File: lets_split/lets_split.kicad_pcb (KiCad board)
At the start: 2 copper layers, 112 x 79 mm, 64 parts, among them J1 3PIN, J2 6PIN, J3 3PIN, J4 CON1, SW1 SW_PUSH, SW10 SW_PUSH, SW11 SW_PUSH, SW12 SW_PUSH, SW13 SW_PUSH, SW14 SW_PUSH, SW15 SW_PUSH, SW16 SW_PUSH, SW17 SW_PUSH, SW18 SW_PUSH, SW19 SW_PUSH, SW2 SW_PUSH, SW20 SW_PUSH, SW21 SW_PUSH, SW22 SW_PUSH, SW23 SW_PUSH, SW24 SW_PUSH, SW3 SW_PUSH, SW4 SW_PUSH, SW5 SW_PUSH, SW6 SW_PUSH, SW7 SW_PUSH, SW8 SW_PUSH, SW9 SW_PUSH, U1 ProMicro, U2 HOLE, U3 HOLE, U4 HOLE, U5 HOLE

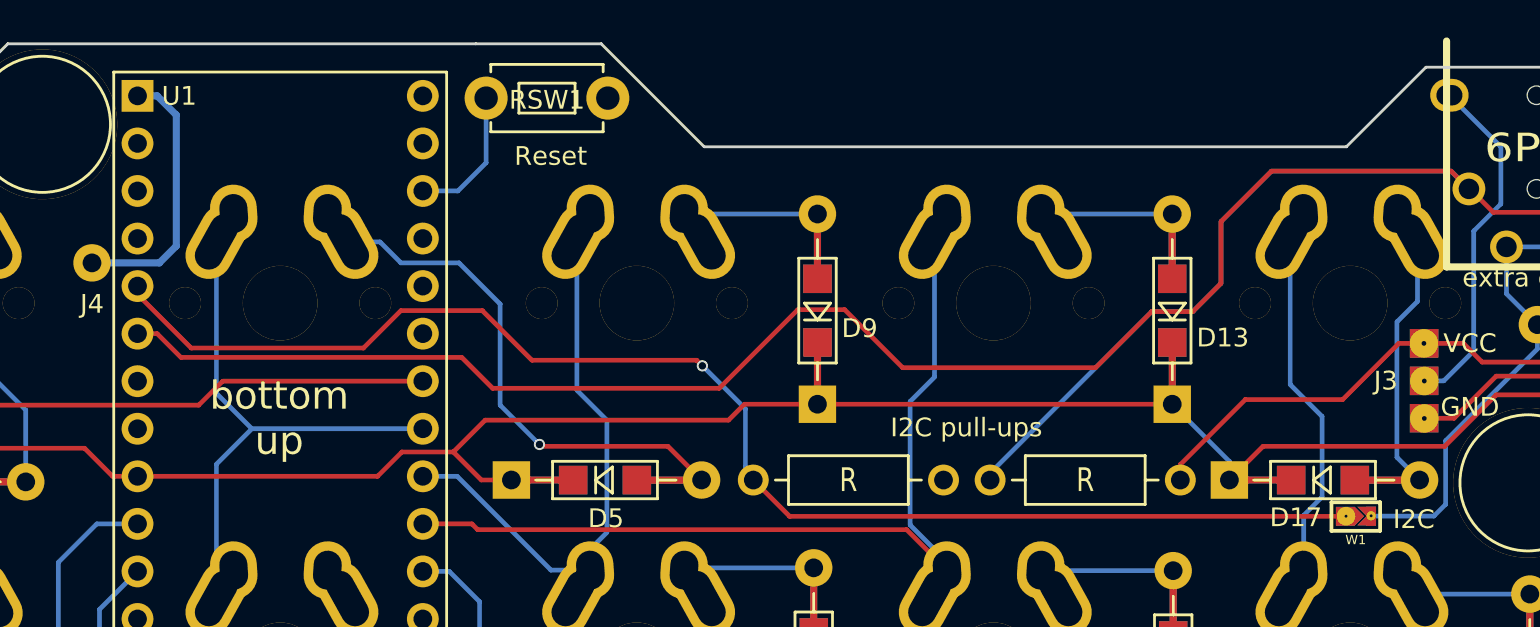
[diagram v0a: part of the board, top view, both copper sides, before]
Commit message: Change bottom fill from VCC to GND
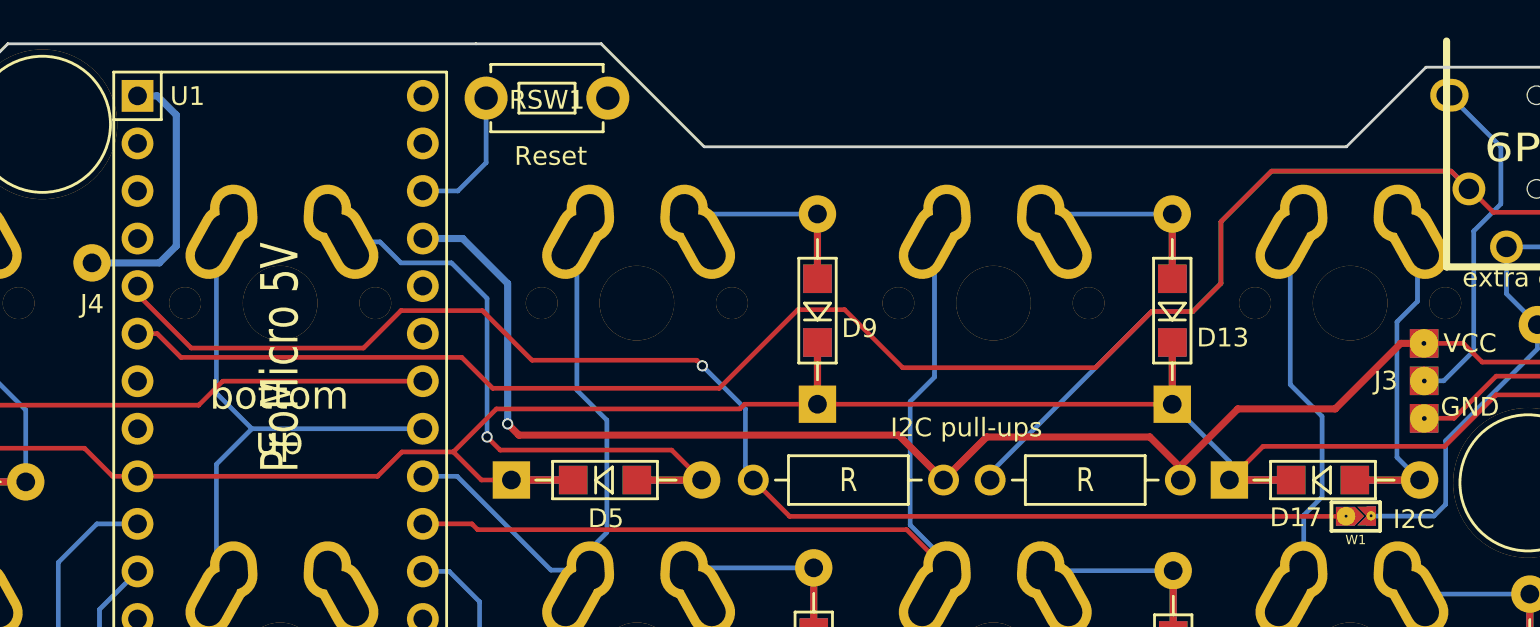
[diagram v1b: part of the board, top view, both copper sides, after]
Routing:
- net VCC: track 29.1 -> 81.5 mm, vias 0 -> 1
- net Net-(D5-Pad2): track 34.3 -> 35.4 mm
- added copper zone on B.Cu, net GND
- removed copper zone on B.Cu, net VCC

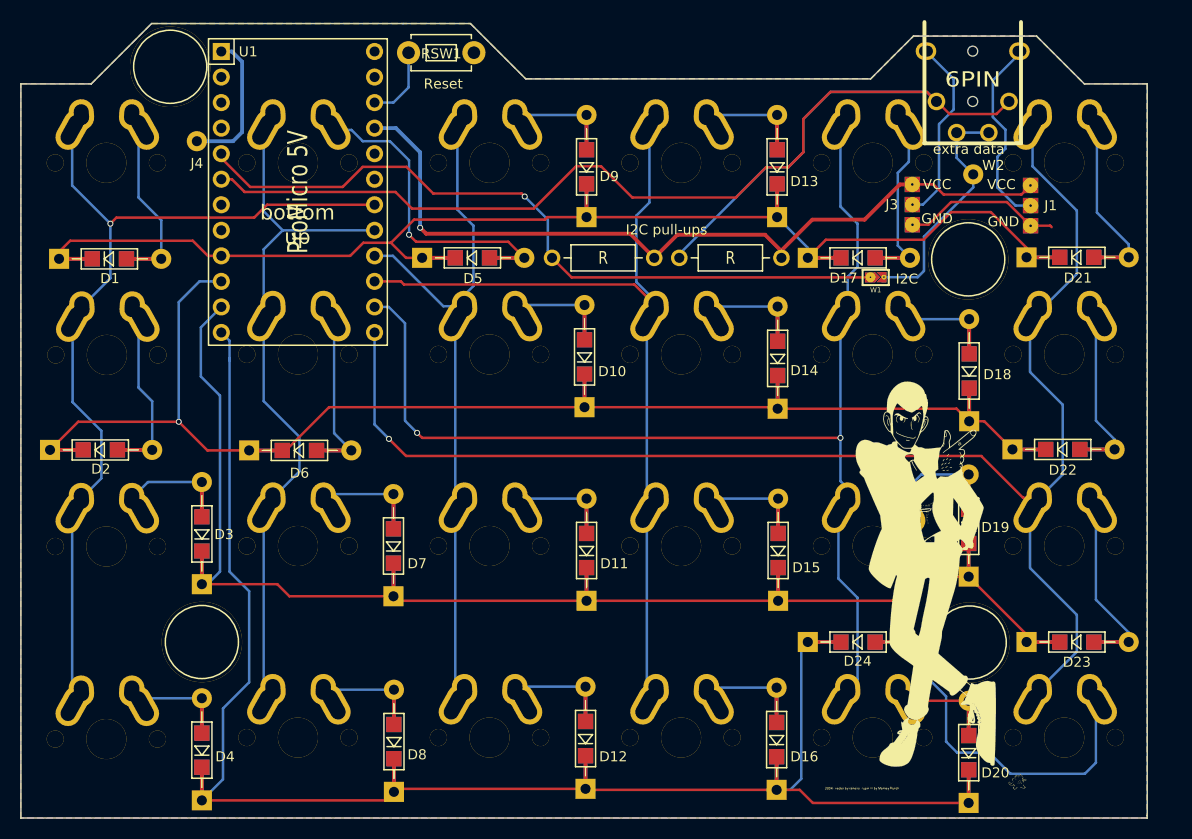
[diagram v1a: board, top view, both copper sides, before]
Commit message: Add pads for RGB LED strip which uses WS2812B for underglow
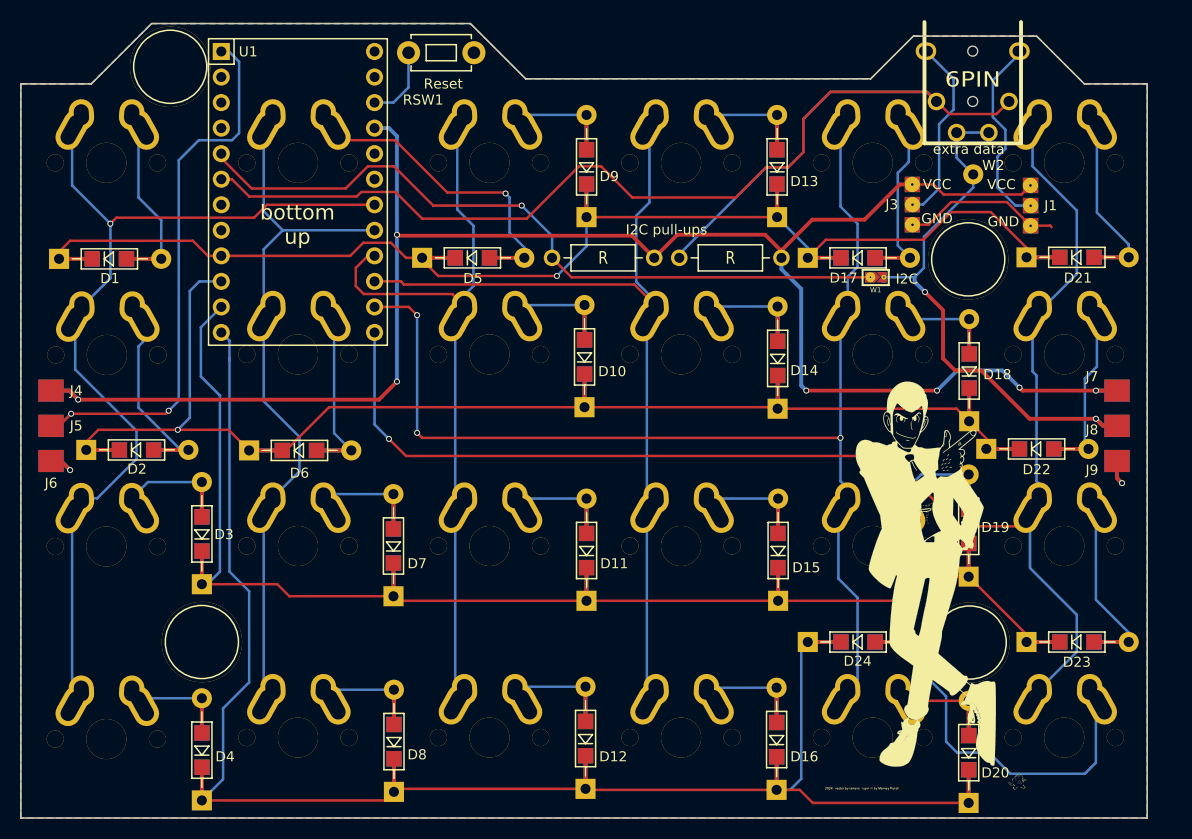
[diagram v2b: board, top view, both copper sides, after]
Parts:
- added J5: CON1, local:CON1_SMD_BOTH, F.Cu at (40.0, 73.0)
- added J6: CON1, local:CON1_SMD_BOTH, F.Cu at (40.0, 76.5)
- added J7: CON1, local:CON1_SMD_BOTH, F.Cu at (146.0, 69.5)
- added J8: CON1, local:CON1_SMD_BOTH, F.Cu at (146.0, 73.0)
- added J9: CON1, local:CON1_SMD_BOTH, F.Cu at (146.0, 76.5)
- J4: footprint local:CON1 -> local:CON1_SMD_BOTH
- moved J4 28.7 mm to (40.0, 69.5)
- moved D2 3.60 mm to (43.5, 75.4)
- moved D22 2.60 mm to (133.0, 75.3)
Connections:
- J4 pad 1: Net-(J4-Pad1) -> VCC
- U1 pad 1: Net-(J4-Pad1) -> Net-(J5-Pad1)
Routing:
- net VCC: track 81.5 -> 184.9 mm, vias 1 -> 7
- net Net-(J5-Pad1): track 0.00 -> 56.5 mm, vias 0 -> 2
- net xtradata: track 23.9 -> 55.4 mm, vias 0 -> 2
- net Net-(J4-Pad1): track 14.4 -> 0.00 mm
- net GND: track 15.8 -> 25.2 mm, vias 0 -> 2
- net row1: track 158.0 -> 153.0 mm
- net col2: track 65.5 -> 70.3 mm
- net col0: track 84.9 -> 88.7 mm
- net Net-(D2-Pad2): track 20.4 -> 22.3 mm
- net Net-(D5-Pad2): track 35.4 -> 33.8 mm
- net data: track 125.2 -> 126.4 mm
- net col4: track 112.8 -> 113.9 mm, vias 2 -> 3
- net col5: track 140.4 -> 139.3 mm
- net row0: track 149.5 -> 150.3 mm, vias 0 -> 1
- net I2C_SDA: track 73.5 -> 73.0 mm
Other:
- board text added: "J5"
- board text added: "J6"
- board text added: "J7"
- board text added: "J8"
- board text added: "J9"

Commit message: Simplify jumper for pin selection of TSSR jack
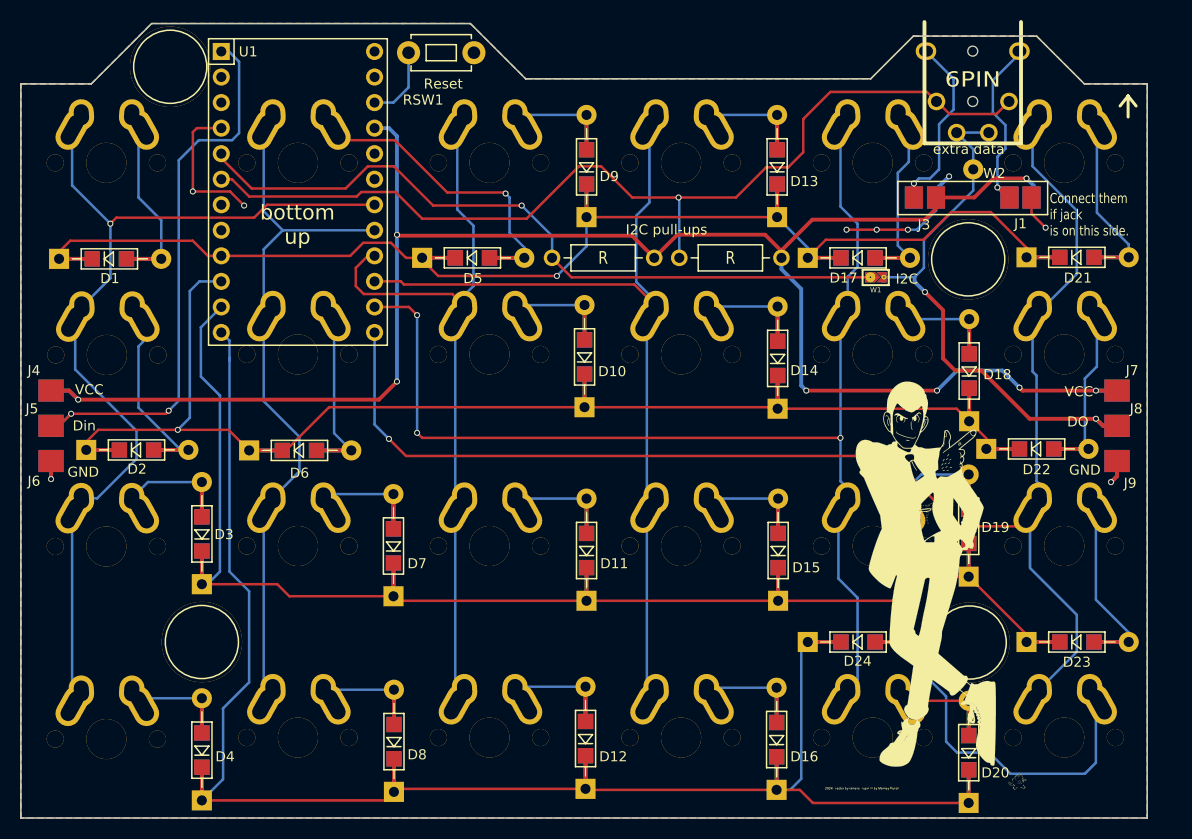
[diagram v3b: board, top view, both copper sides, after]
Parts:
- J1: footprint prettylib:jumper -> local:SMD_JUMPER_2
- J3: footprint prettylib:jumper -> local:SMD_JUMPER_2; moved to B.Cu
- moved J1 3.10 mm to (136.4, 50.3), turned to 0 degrees
- moved J3 1.03 mm to (126.9, 50.3), turned to 0 degrees
- moved W2 0.50 mm to (131.7, 47.5)
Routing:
- net data: track 126.4 -> 97.5 mm, vias 0 -> 1
- net GND: track 25.2 -> 40.0 mm, vias 2 -> 9
- net VCC: track 184.9 -> 187.1 mm, vias 7 -> 8
- net Net-(J1-Pad2): track 19.5 -> 18.7 mm, vias 0 -> 1
- net Net-(J2-Pad4): track 18.7 -> 19.4 mm, vias 0 -> 1
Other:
- board text added: "Connect them if jack is on this side."
- board text added: "DO"
- board text added: "Designed by Wootpatoot"
- board text added: "Din"
- board text added: "J1"
- board text added: "J3"
- board text removed: "By Wootpatoot"

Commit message: Add some GND fill
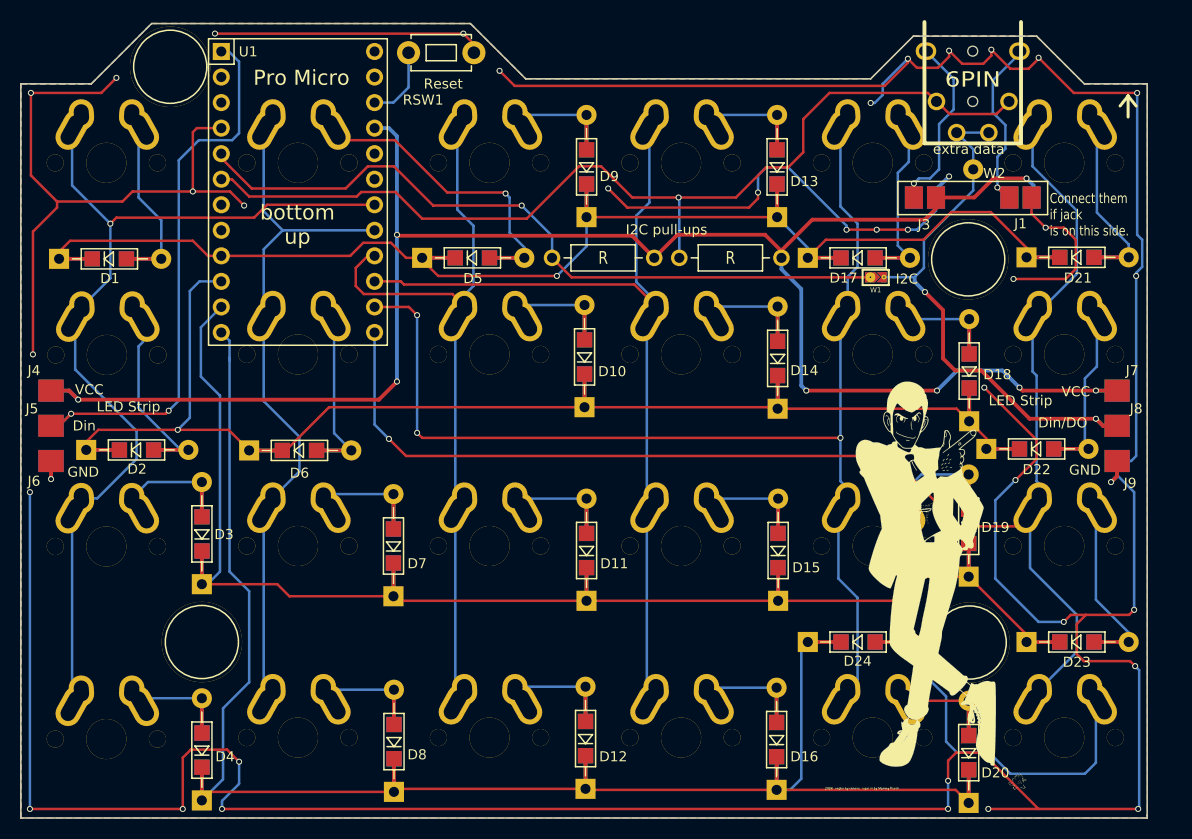
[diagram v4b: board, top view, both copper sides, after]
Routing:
- net GND: track 40.0 -> 523.9 mm, vias 9 -> 39
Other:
- board text added: "DO/Din"
- board text added: "Din/DO"
- board text added: "LED Strip"
- board text added: "Pro Micro"
- board text added: "U1"
- board text removed: "DO"

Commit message: Replace switch module without oval holes
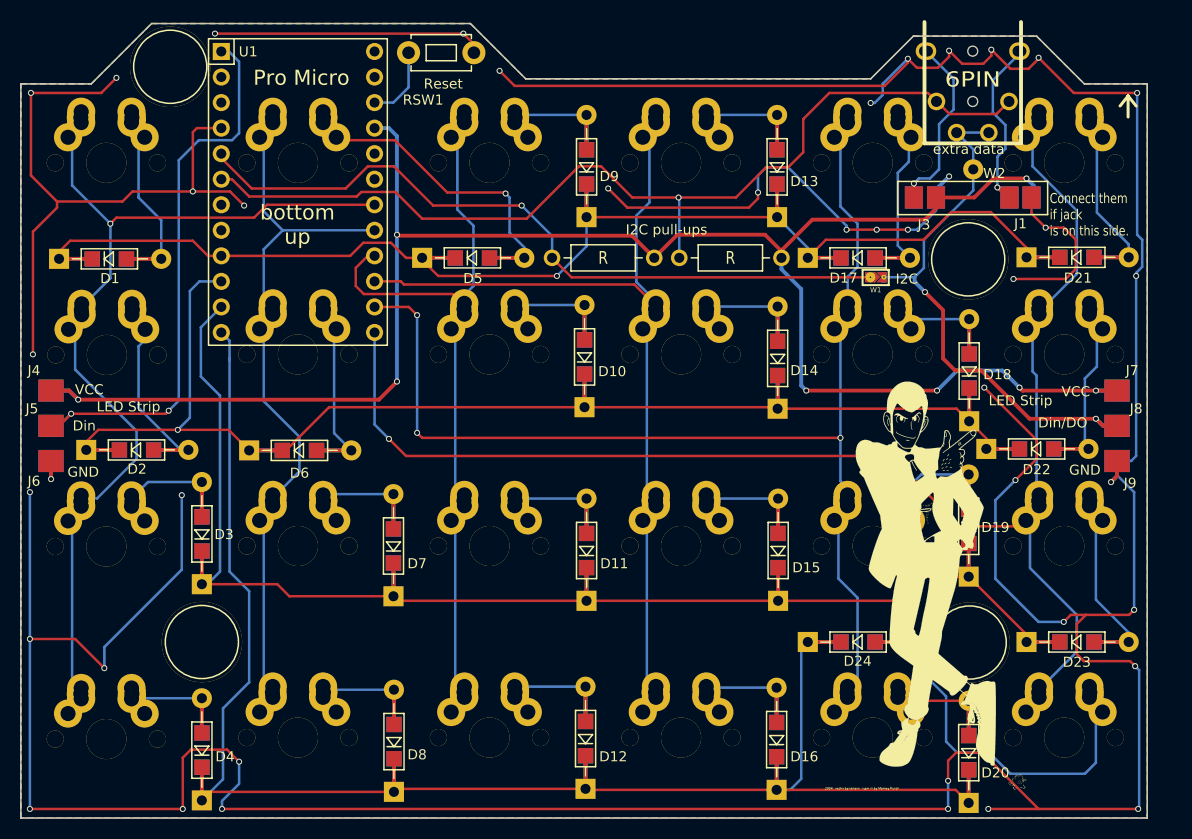
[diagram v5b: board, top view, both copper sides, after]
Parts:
- SW1, SW10, SW11, SW12, SW13, SW14, SW15, SW16, SW17, SW18, SW19, SW2, SW20, SW21, SW22, SW23, SW24, SW3, SW4, SW5, SW6, SW7, SW8, SW9: footprint flipalps:MXALPS_FLIP -> local:MXALPS_FLIP_HOLES
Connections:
- U1 pad 19: (no net) -> Net-(U1-Pad19)
- U1 pad 2: (no net) -> Net-(U1-Pad2)
- U1 pad 20: (no net) -> Net-(U1-Pad20)
- U1 pad 24: (no net) -> Net-(U1-Pad24)
- U1 pad 7: (no net) -> Net-(U1-Pad7)
- U1 pad 8: (no net) -> Net-(U1-Pad8)
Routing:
- net GND: track 523.9 -> 552.9 mm, vias 39 -> 42
- net col5: track 139.3 -> 141.8 mm
- net col2: track 70.3 -> 72.8 mm
- net col1: track 66.6 -> 69.1 mm
- net col0: track 88.7 -> 91.2 mm
- net col3: track 83.8 -> 86.3 mm
- net col4: track 113.9 -> 116.4 mm

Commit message: Add fiducial marks
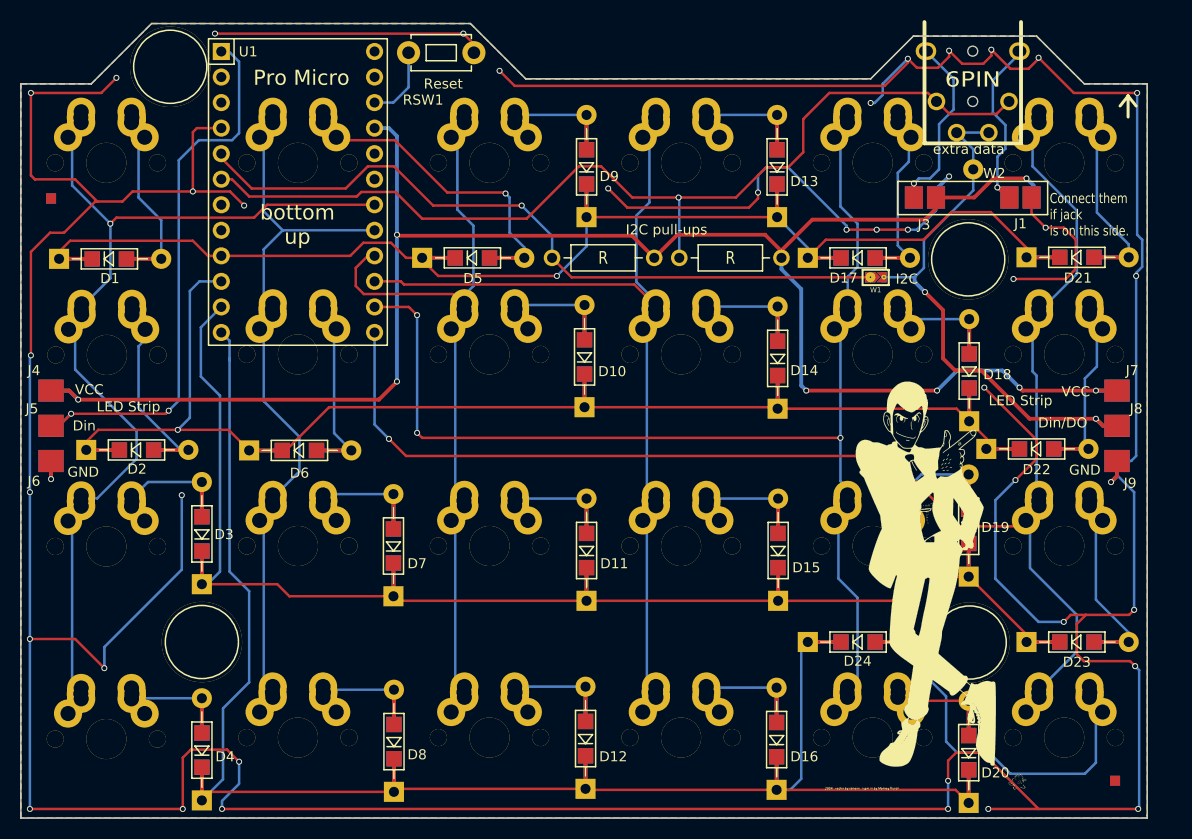
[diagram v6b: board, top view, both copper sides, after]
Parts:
- added M1: FIDUCIAL, local:Fiducial_Mark, F.Cu at (40.0, 50.4)
- added M2: FIDUCIAL, local:Fiducial_Mark, F.Cu at (145.8, 108.3)
- added M3: FIDUCIAL, local:Fiducial_Mark, B.Cu at (145.8, 108.3)
- added M4: FIDUCIAL, local:Fiducial_Mark, B.Cu at (40.0, 50.4)
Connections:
- U1 pad 19: Net-(U1-Pad19) -> (no net)
- U1 pad 2: Net-(U1-Pad2) -> (no net)
- U1 pad 20: Net-(U1-Pad20) -> (no net)
- U1 pad 24: Net-(U1-Pad24) -> (no net)
- U1 pad 7: Net-(U1-Pad7) -> (no net)
- U1 pad 8: Net-(U1-Pad8) -> (no net)
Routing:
- net GND: track 552.9 -> 569.3 mm

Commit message: Fix to match the distance between switch and side edge on both sides
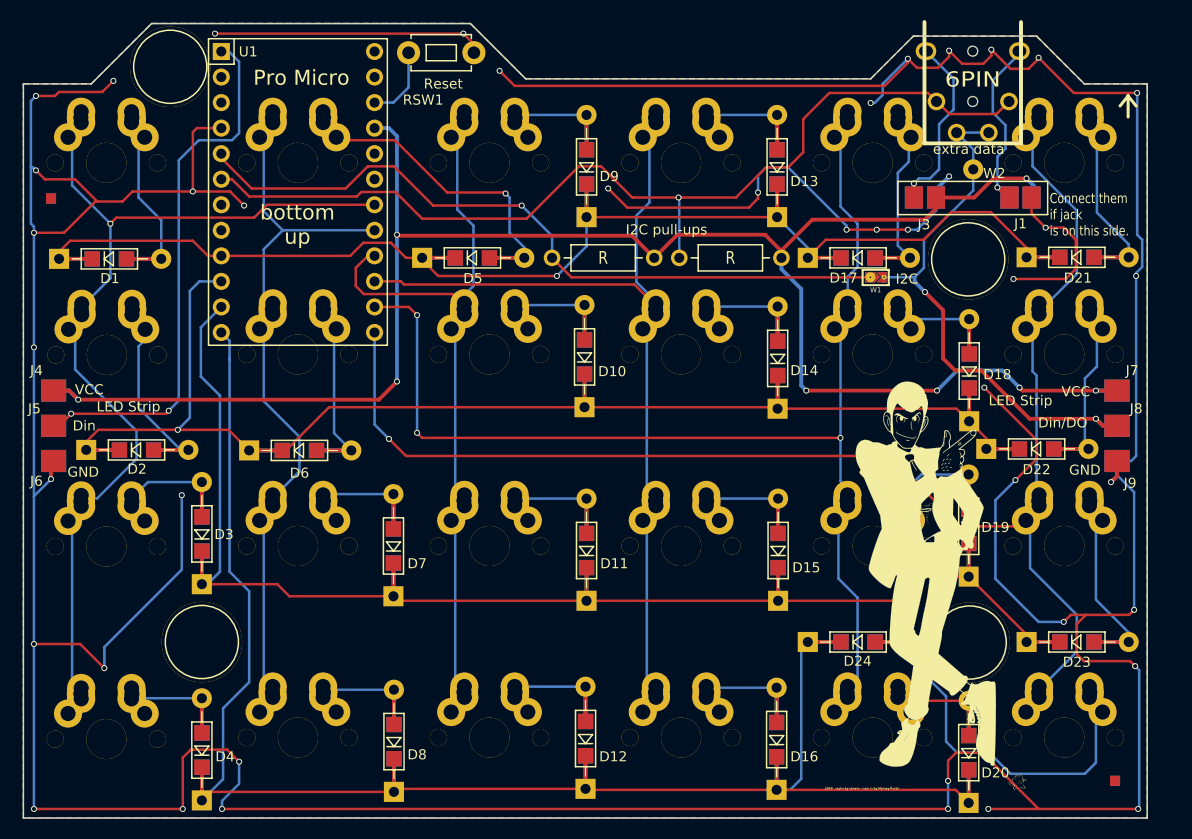
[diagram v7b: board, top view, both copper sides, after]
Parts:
- moved J4 0.25 mm to (40.2, 69.5)
- moved J5 0.25 mm to (40.2, 73.0)
- moved J6 0.25 mm to (40.2, 76.5)
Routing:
- net GND: track 569.3 -> 576.7 mm, vias 42 -> 43
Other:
- board size 112 x 79 mm -> 111.8 x 79 mm
